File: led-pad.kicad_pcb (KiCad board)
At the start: 2 copper layers, 19 x 28.5 mm, 10 parts, among them J1 Conn_01x04_Socket, J2 Conn_01x06_Socket

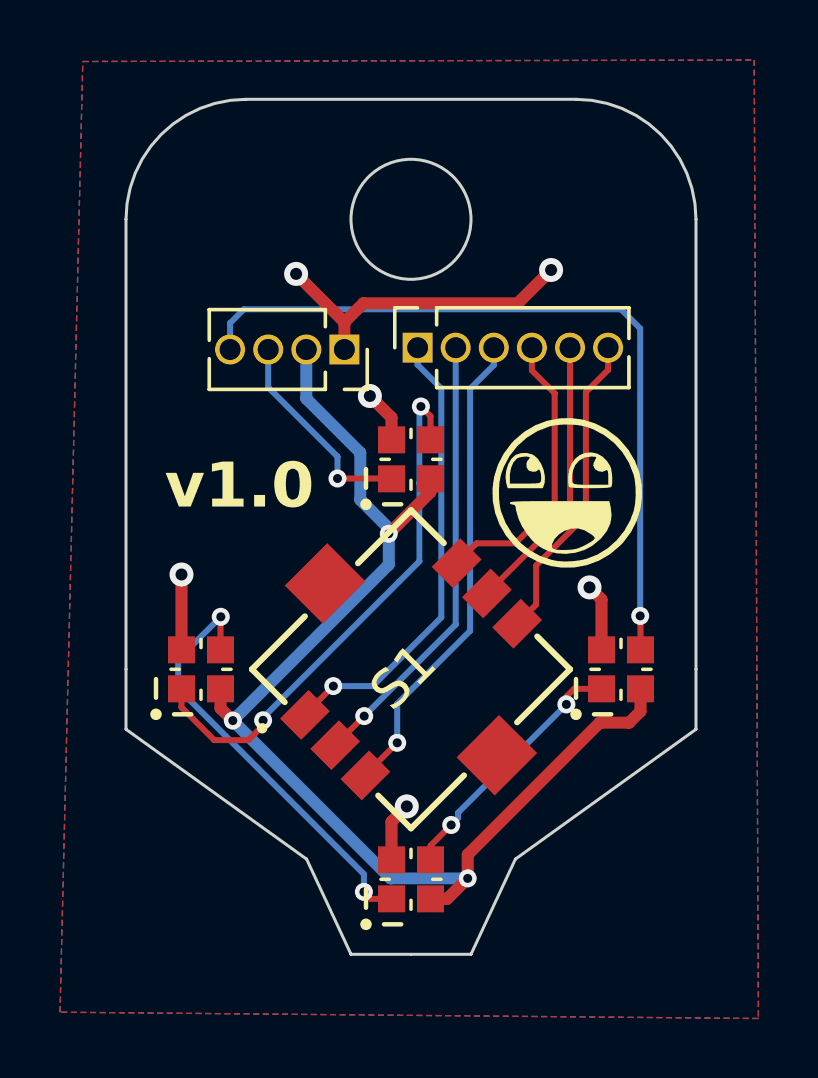
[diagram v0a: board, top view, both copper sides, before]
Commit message: reworking for ffc connector, adding step file
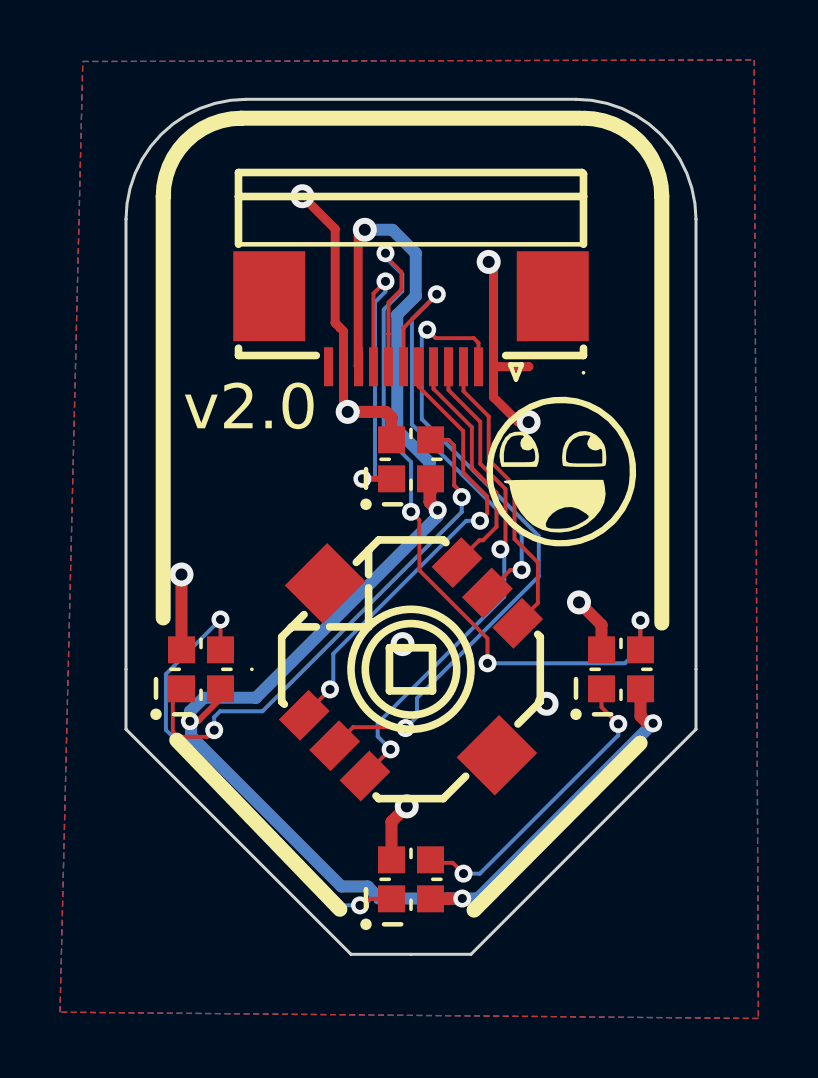
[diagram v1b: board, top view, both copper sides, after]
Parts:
- removed J2: Conn_01x06_Socket, Connector_PinSocket_1.27mm:PinSocket_1x06_P1.27mm_Vertical
- J1: value Conn_01x04_Socket -> vik-module-connector; footprint Connector_PinSocket_1.27mm:PinSocket_1x04_P1.27mm_Vertical -> kicad-libraries:FFC-SMD_FFC05001-12SBA124W5M
- S1: footprint ct-kicad:SKRHAAE010 -> kicad-libraries:SW-SMD_SKRHACE010
- moved LOGO3 9.79 mm to (152.4, 87.8)
- moved LOGO2 8.73 mm to (149.8, 105.0)
- moved J1 2.30 mm to (150.0, 88.7), turned to 180 degrees
- moved LOGO1 0.74 mm to (155.0, 93.4)
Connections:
- J1 pad 2: +5V -> CENTER
- J1 pad 3: DI -> D
- J1 pad 4: DO -> C
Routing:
- net +5V: track 40.1 -> 53.4 mm, vias 3 -> 5
- net CENTER: track 14.9 -> 22.1 mm, vias 1 -> 2
- net COM: track 9.34 -> 15.4 mm, vias 0 -> 2
- net GND: track 19.3 -> 23.9 mm, vias 6 -> 9
- net DI: track 7.06 -> 11.1 mm, vias 1 -> 2
- net B: track 9.61 -> 8.01 mm
- net Net-(D3-DOUT): track 8.59 -> 10.1 mm
- net DO: track 25.7 -> 27.0 mm, vias 1 -> 4
- net Net-(D2-DOUT): track 14.4 -> 15.5 mm
- net C: track 16.0 -> 16.8 mm, vias 1 -> 2
- net D: track 10.5 -> 9.86 mm
- net A: track 15.2 -> 15.3 mm, vias 1 -> 2
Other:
- outline, holes or cut-outs redrawn
- board text added: "v2.0"
- board text removed: "v1.0"
